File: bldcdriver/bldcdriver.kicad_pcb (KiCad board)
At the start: 2 copper layers, 107 x 75 mm, 11 parts, among them Q1 IRF3205, Q2 IRF3205, Q3 IRF3205, Q4 IRF3205, Q5 IRF3205, Q6 IRF3205, U1 DRV8304SRHAR, U2 RP2040

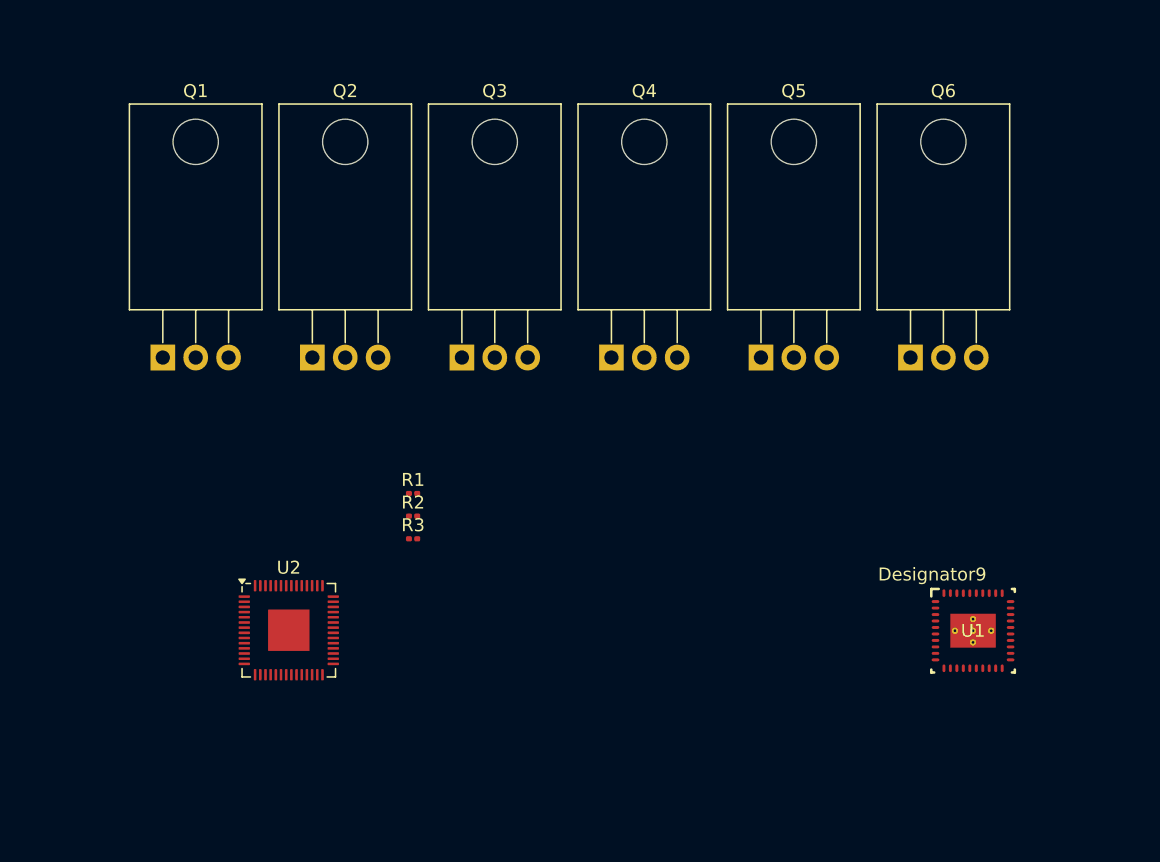
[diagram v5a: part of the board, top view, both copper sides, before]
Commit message: Added the QSPI chip but not fully interfaced with the button/jumper, added decoupling capacitors for the RP2040
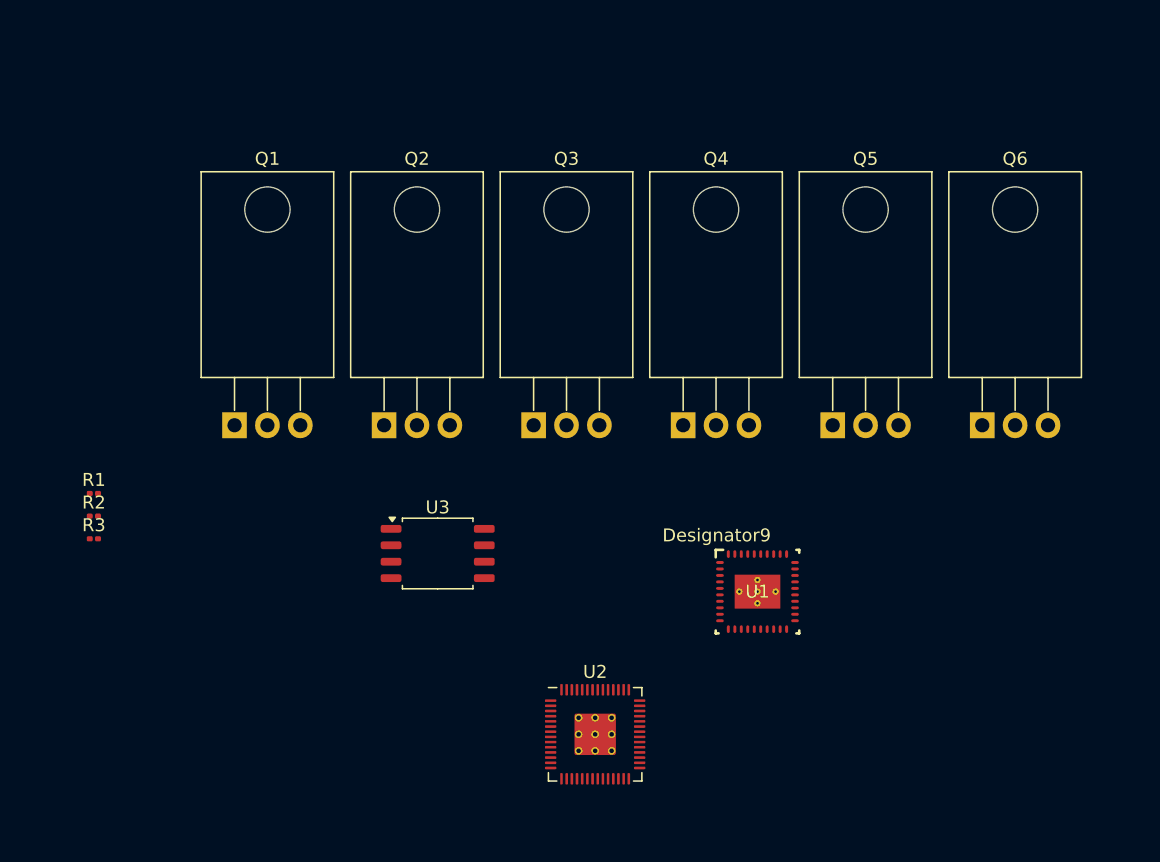
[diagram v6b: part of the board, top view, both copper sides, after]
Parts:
- added U3: W25Q128JVS, Package_SO:SOIC-8_5.23x5.23mm_P1.27mm, F.Cu at (108.9, 98.1)
- U2: footprint Package_DFN_QFN:QFN-56-1EP_7x7mm_P0.4mm_EP3.2x3.2mm -> RP2040:RP2040-QFN-56
- moved U2 25.0 mm to (121.1, 112.1)
- moved R1 24.7 mm to (82.3, 93.5)
- moved R2 24.7 mm to (82.3, 95.2)
- moved R3 24.7 mm to (82.3, 97.0)
- moved U1 16.9 mm to (133.6, 101.1)
- moved Q6 7.62 mm to (151.0, 88.2)
- moved Q2 7.62 mm to (104.8, 88.2)
- moved Q3 7.62 mm to (116.3, 88.2)
- moved Q4 7.62 mm to (127.9, 88.2)
- moved Q1 7.62 mm to (93.2, 88.2)
- moved Q5 7.62 mm to (139.4, 88.2)
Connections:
- Q1 pad 1: /GHA -> /Three Phase Half Bridge/GHA
- Q1 pad 3: /Phase A -> /Three Phase Half Bridge/Phase A
- Q2 pad 1: /GLA -> /Three Phase Half Bridge/GLA
- Q2 pad 2: /Phase A -> /Three Phase Half Bridge/Phase A
- Q2 pad 3: /SPA -> /Three Phase Half Bridge/SPA
- Q3 pad 1: /GHB -> /Three Phase Half Bridge/GHB
- Q3 pad 3: /Phase B -> /Three Phase Half Bridge/Phase B
- Q4 pad 1: /GLB -> /Three Phase Half Bridge/GLB
- Q4 pad 2: /Phase B -> /Three Phase Half Bridge/Phase B
- Q4 pad 3: /SPB -> /Three Phase Half Bridge/SPB
- Q5 pad 1: /GHC -> /Three Phase Half Bridge/GHC
- Q5 pad 3: /Phase C -> /Three Phase Half Bridge/Phase C
- Q6 pad 1: /GLC -> /Three Phase Half Bridge/GLC
- Q6 pad 2: /Phase C -> /Three Phase Half Bridge/Phase C
- Q6 pad 3: /SPC -> /Three Phase Half Bridge/SPC
- R1 pad 1: /SPA -> /Three Phase Half Bridge/SPA
- R2 pad 1: /SPB -> /Three Phase Half Bridge/SPB
- R3 pad 1: /SPC -> /Three Phase Half Bridge/SPC
- U1 pad 12: /SPB -> /DRV Sheet/SPB
- U1 pad 13: /GLB -> /DRV Sheet/GLB
- U1 pad 14: /Phase B -> /DRV Sheet/SHB
- U1 pad 15: /GHB -> /DRV Sheet/GHB
- U1 pad 16: /GHC -> /DRV Sheet/GHC
- U1 pad 17: /Phase C -> /DRV Sheet/SHC
- U1 pad 18: /GLC -> /DRV Sheet/GLC
- U1 pad 19: /SPC -> /DRV Sheet/SPC
- U1 pad 6: /GHA -> /DRV Sheet/GHA
- U1 pad 7: /Phase A -> /DRV Sheet/SHA
- U1 pad 8: /GLA -> /DRV Sheet/GLA
- U1 pad 9: /SPA -> /DRV Sheet/SPA
- U2 pad 1: Net-(U2-IOVDD-Pad1) -> +3.3V
- U2 pad 10: Net-(U2-IOVDD-Pad1) -> +3.3V
- U2 pad 19: unconnected-(U2-TESTEN-Pad19) -> GND
- U2 pad 22: Net-(U2-IOVDD-Pad1) -> +3.3V
- U2 pad 23: Net-(U2-DVDD-Pad23) -> +1V1
- U2 pad 33: Net-(U2-IOVDD-Pad1) -> +3.3V
- U2 pad 42: Net-(U2-IOVDD-Pad1) -> +3.3V
- U2 pad 43: unconnected-(U2-ADC_AVDD-Pad43) -> +3.3V
- U2 pad 44: unconnected-(U2-VREG_IN-Pad44) -> +3.3V
- U2 pad 45: unconnected-(U2-VREG_VOUT-Pad45) -> +1V1
- U2 pad 48: unconnected-(U2-USB_VDD-Pad48) -> +3.3V
- U2 pad 49: Net-(U2-IOVDD-Pad1) -> +3.3V
- U2 pad 50: Net-(U2-DVDD-Pad23) -> +1V1
- U2 pad 51: unconnected-(U2-QSPI_SD3-Pad51) -> /rp2040_sheet/QSPI_SD3
- U2 pad 52: unconnected-(U2-QSPI_SCLK-Pad52) -> /rp2040_sheet/QSPI_SCLK
- U2 pad 53: unconnected-(U2-QSPI_SD0-Pad53) -> /rp2040_sheet/QSPI_SD0
- U2 pad 54: unconnected-(U2-QSPI_SD2-Pad54) -> /rp2040_sheet/QSPI_SD2
- U2 pad 55: unconnected-(U2-QSPI_SD1-Pad55) -> /rp2040_sheet/QSPI_SD1
- U2 pad 56: unconnected-(U2-QSPI_SS-Pad56) -> /rp2040_sheet/QSPI_SS

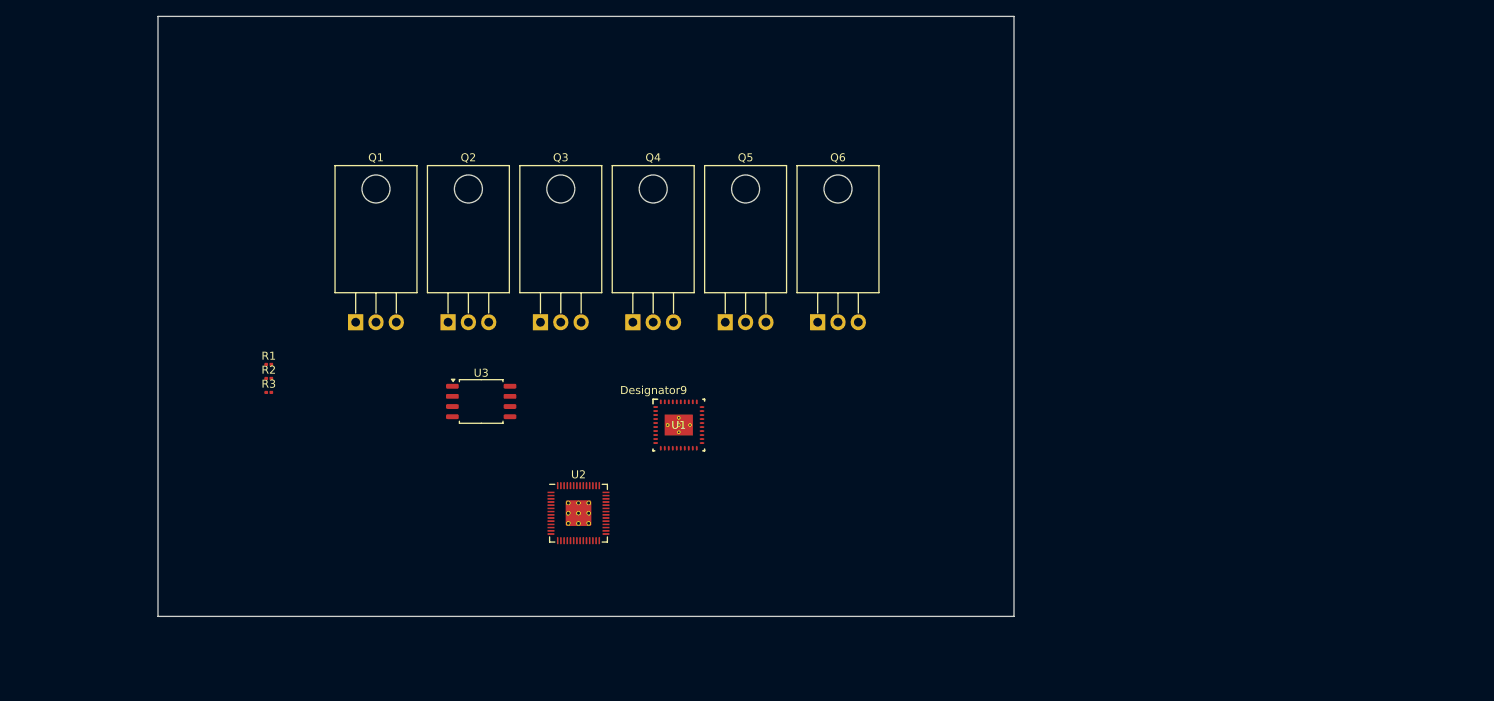
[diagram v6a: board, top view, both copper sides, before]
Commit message: Added a USB C Connector and wired it up to act as USB 2.0
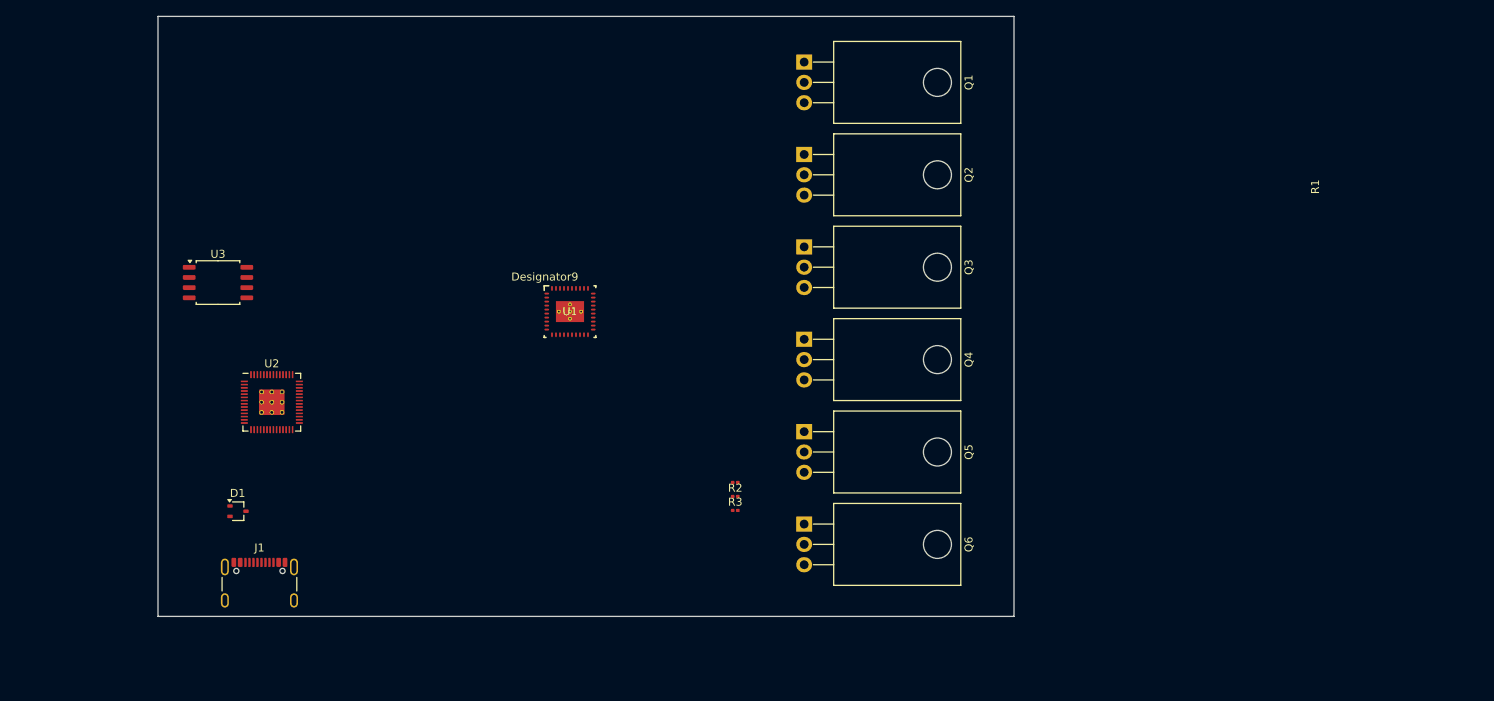
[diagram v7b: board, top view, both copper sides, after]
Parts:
- added D1: BAT54W, Package_TO_SOT_SMD:SOT-323_SC-70, F.Cu at (78.5, 111.8)
- added J1: USB_C_Receptacle_USB2.0_14P, Connector_USB:USB_C_Receptacle_GCT_USB4105-xx-A_16P_TopMnt_Horizontal, F.Cu at (81.2, 121.9)
- moved Q1 64.8 mm to (149.3, 55.7), turned to -90 degrees
- moved R1 60.1 mm to (140.7, 108.2)
- moved R2 60.1 mm to (140.7, 110.0)
- moved R3 60.1 mm to (140.7, 111.8)
- moved Q2 49.2 mm to (149.3, 67.3), turned to -90 degrees
- moved U2 40.8 mm to (82.7, 98.2)
- moved U3 36.1 mm to (76.0, 83.3)
- moved Q3 34.3 mm to (149.3, 78.8), turned to -90 degrees
- moved Q6 25.3 mm to (149.3, 113.5), turned to -90 degrees
- moved Q4 21.5 mm to (149.3, 90.4), turned to -90 degrees
- moved U1 19.6 mm to (120.0, 86.9)
- moved Q5 16.9 mm to (149.3, 101.9), turned to -90 degrees
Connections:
- U2 pad 46: unconnected-(U2-USB_DM-Pad46) -> Net-(U2-USB_DM)
- U2 pad 47: unconnected-(U2-USB_DP-Pad47) -> Net-(U2-USB_DP)

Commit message: Increased main sheet size to A2 and fit everything there
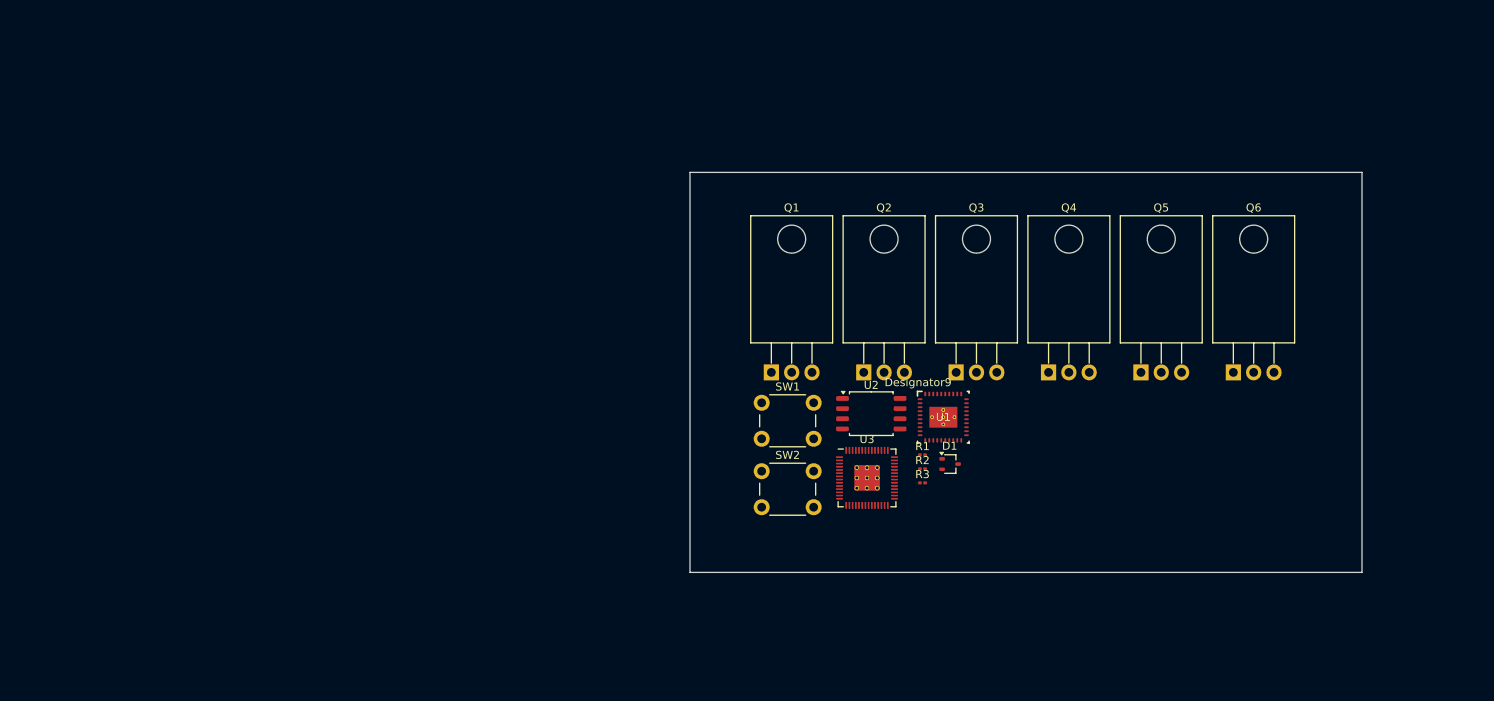
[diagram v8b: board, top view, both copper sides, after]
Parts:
- removed J1: USB_C_Receptacle_USB2.0_14P, Connector_USB:USB_C_Receptacle_GCT_USB4105-xx-A_16P_TopMnt_Horizontal
- added SW1: SW_Push, Button_Switch_THT:SW_PUSH_6mm, F.Cu at (144.0, 98.3)
- added SW2: SW_Push, Button_Switch_THT:SW_PUSH_6mm, F.Cu at (144.0, 106.8)
- U2: value RP2040 -> W25Q128JVS; footprint RP2040:RP2040-QFN-56 -> Package_SO:SOIC-8_5.23x5.23mm_P1.27mm
- U3: value W25Q128JVS -> RP2040; footprint Package_SO:SOIC-8_5.23x5.23mm_P1.27mm -> RP2040:RP2040-QFN-56
- moved D1 89.2 mm to (167.5, 106.0)
- moved U3 84.7 mm to (157.1, 107.7)
- moved U2 74.9 mm to (157.7, 99.7)
- moved Q6 56.9 mm to (202.9, 94.5), turned to 0 degrees
- moved U1 48.5 mm to (166.7, 100.1)
- moved Q5 42.7 mm to (191.4, 94.5), turned to 0 degrees
- moved Q1 39.0 mm to (145.2, 94.5), turned to 0 degrees
- moved Q4 30.8 mm to (179.8, 94.5), turned to 0 degrees
- moved Q2 28.2 mm to (156.7, 94.5), turned to 0 degrees
- moved Q3 24.6 mm to (168.3, 94.5), turned to 0 degrees
- moved R1 23.7 mm to (164.1, 104.8)
- moved R2 23.7 mm to (164.1, 106.5)
- moved R3 23.7 mm to (164.1, 108.3)
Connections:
- Q1 pad 1: /Three Phase Half Bridge/GHA -> /GHA
- Q1 pad 3: /Three Phase Half Bridge/Phase A -> /Phase A
- Q2 pad 1: /Three Phase Half Bridge/GLA -> /GLA
- Q2 pad 2: /Three Phase Half Bridge/Phase A -> /Phase A
- Q2 pad 3: /Three Phase Half Bridge/SPA -> /SPA
- Q3 pad 1: /Three Phase Half Bridge/GHB -> /GHB
- Q3 pad 3: /Three Phase Half Bridge/Phase B -> /Phase B
- Q4 pad 1: /Three Phase Half Bridge/GLB -> /GLB
- Q4 pad 2: /Three Phase Half Bridge/Phase B -> /Phase B
- Q4 pad 3: /Three Phase Half Bridge/SPB -> /SPB
- Q5 pad 1: /Three Phase Half Bridge/GHC -> /GHC
- Q5 pad 3: /Three Phase Half Bridge/Phase C -> /Phase C
- Q6 pad 1: /Three Phase Half Bridge/GLC -> /GLC
- Q6 pad 2: /Three Phase Half Bridge/Phase C -> /Phase C
- Q6 pad 3: /Three Phase Half Bridge/SPC -> /SPC
- R1 pad 1: /Three Phase Half Bridge/SPA -> /SPA
- R2 pad 1: /Three Phase Half Bridge/SPB -> /SPB
- R3 pad 1: /Three Phase Half Bridge/SPC -> /SPC
- U1 pad 12: /DRV Sheet/SPB -> /SPB
- U1 pad 13: /DRV Sheet/GLB -> /GLB
- U1 pad 14: /DRV Sheet/SHB -> /Phase B
- U1 pad 15: /DRV Sheet/GHB -> /GHB
- U1 pad 16: /DRV Sheet/GHC -> /GHC
- U1 pad 17: /DRV Sheet/SHC -> /Phase C
- U1 pad 18: /DRV Sheet/GLC -> /GLC
- U1 pad 19: /DRV Sheet/SPC -> /SPC
- U1 pad 21: unconnected-(U1-SOC-Pad21) -> Net-(J2-Pin_1)
- U1 pad 22: unconnected-(U1-SOB-Pad22) -> Net-(J2-Pin_2)
- U1 pad 23: unconnected-(U1-SOA-Pad23) -> Net-(J2-Pin_3)
- U1 pad 25: unconnected-(U1-FAULT_N-Pad25) -> /nFAULT
- U1 pad 26: unconnected-(U1-SDO-Pad26) -> /SPI_SDI
- U1 pad 27: unconnected-(U1-SDI-Pad27) -> /SPI_SDO
- U1 pad 28: unconnected-(U1-SCLK-Pad28) -> /SPI_CLK
- U1 pad 29: unconnected-(U1-SCS_N-Pad29) -> /SPI_CSn_DRV
- U1 pad 30: unconnected-(U1-ENABLE-Pad30) -> /DREN
- U1 pad 34: unconnected-(U1-INHA-Pad34) -> /INHA
- U1 pad 35: unconnected-(U1-INLA-Pad35) -> /INLA
- U1 pad 36: unconnected-(U1-INHB-Pad36) -> /INHB
- U1 pad 37: unconnected-(U1-INLB-Pad37) -> /INLB
- U1 pad 38: unconnected-(U1-INHC-Pad38) -> /INHC
- U1 pad 39: unconnected-(U1-INLC-Pad39) -> /INLC
- U1 pad 6: /DRV Sheet/GHA -> /GHA
- U1 pad 7: /DRV Sheet/SHA -> /Phase A
- U1 pad 8: /DRV Sheet/GLA -> /GLA
- U1 pad 9: /DRV Sheet/SPA -> /SPA
- U2 pad 1: +3.3V -> /QSPI_SS
- U2 pad 2: unconnected-(U2-GPIO0-Pad2) -> /QSPI_SD1
- U2 pad 3: unconnected-(U2-GPIO1-Pad3) -> /QSPI_SD2
- U2 pad 4: unconnected-(U2-GPIO2-Pad4) -> GND
- U2 pad 5: unconnected-(U2-GPIO3-Pad5) -> /QSPI_SD0
- U2 pad 6: unconnected-(U2-GPIO4-Pad6) -> /QSPI_SCLK
- U2 pad 7: unconnected-(U2-GPIO5-Pad7) -> /QSPI_SD3
- U2 pad 8: unconnected-(U2-GPIO6-Pad8) -> +3.3V
- U3 pad 1: /rp2040_sheet/QSPI_SS -> +3.3V
- U3 pad 2: /rp2040_sheet/QSPI_SD1 -> /INHA
- U3 pad 3: /rp2040_sheet/QSPI_SD2 -> /INLA
- U3 pad 4: GND -> /INHB
- U3 pad 5: /rp2040_sheet/QSPI_SD0 -> /INLB
- U3 pad 6: /rp2040_sheet/QSPI_SCLK -> /INHC
- U3 pad 7: /rp2040_sheet/QSPI_SD3 -> /INLC
- U3 pad 8: +3.3V -> /DREN
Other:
- board size 107 x 75 mm -> 84 x 50 mm
